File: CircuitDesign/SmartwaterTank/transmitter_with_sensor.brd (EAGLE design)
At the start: 53 x 25.4 mm, 11 parts, among them IC1 MEGA8-P

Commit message: Issue #5: update transmitter schema
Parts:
- added C1, C2: 22pf, rcl:C025-025X050
- added Q1: 455E, special:QS
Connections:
- new net N$10: IC1.6, J_ULTRASONIC_1.ECHO
- new net N$7: C1.1, IC1.9, Q1.2
- new net N$8: C2.1, IC1.10, Q1.1
- new net N$9: IC1.14, U$1.DATA
- net GND: now also C1.2, C2.2
- net N$11: now also IC1.5
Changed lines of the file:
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@@
 <attribute name="VALUE" x="58.42" y="69.18" size="0.0254" layer="27"/>
+</element>
+<element name="Q1" library="special" library_urn="urn:adsk.eagle:library:367" package="QS" package3d_urn="urn:adsk.eagle:package:26647/2" value="455E" x="54.61" y="49.53" smashed="yes">
+<attribute name="NAME" x="49.53" y="52.197" size="1.27" layer="25" ratio="10"/>
+<attribute name="POPULARITY" value="59" x="54.61" y="49.53" size="1.778" layer="27" display="off"/>
+<attribute name="VALUE" x="49.53" y="45.593" size="1.27" layer="27" ratio="10"/>
+</element>
+<element name="C1" library="rcl" library_urn="urn:adsk.eagle:library:334" package="C025-025X050" package3d_urn="urn:adsk.eagle:package:23629/2" value="22pf" x="52.07" y="43.18" smashed="yes">
+<attribute name="NAME" x="49.784" y="44.704" size="1.27" layer="25" ratio="10"/>
+<attribute name="POPULARITY" value="65" x="52.07" y="43.18" size="1.778" layer="27" display="off"/>
+<attribute name="SPICEPREFIX" value="C" x="52.07" y="43.18" size="1.778" layer="27" display="off"/>
+<attribute name="VALUE" x="49.784" y="40.386" size="1.27" layer="27" ratio="10"/>
+</element>
+<element name="C2" library="rcl" library_urn="urn:adsk.eagle:library:334" package="C025-025X050" package3d_urn="urn:adsk.eagle:package:23629/2" value="22pf" x="52.07" y="38.1" smashed="yes">
+<attribute name="NAME" x="49.784" y="39.624" size="1.27" layer="25" ratio="10"/>
+<attribute name="POPULARITY" value="65" x="52.07" y="38.1" size="1.778" layer="27" display="off"/>
+<attribute name="SPICEPREFIX" value="C" x="52.07" y="38.1" size="1.778" layer="27" display="off"/>
+<attribute name="VALUE" x="49.784" y="35.306" size="1.27" layer="27" ratio="10"/>
 </element>
 </elements>
@@
 <signal name="GND">
 <contactref element="IC1" pad="8"/>
+<contactref element="C1" pad="2"/>
+<contactref element="C2" pad="2"/>
+<wire x1="53.34" y1="43.18" x2="81.28" y2="68.58" width="0" layer="19" extent="1-1"/>
+<wire x1="53.34" y1="38.1" x2="53.34" y2="43.18" width="0" layer="19" extent="1-1"/>
 </signal>
 <signal name="AVCC">
@@
 <signal name="N$11">
 <contactref element="J_ULTRASONIC_1" pad="TRIG"/>
+<contactref element="IC1" pad="5"/>
+<wire x1="71.12" y1="62.23" x2="73.66" y2="68.58" width="0" layer="19" extent="1-1"/>
 </signal>
 <signal name="N$1">
@@
 <wire x1="78.74" y1="78.74" x2="78.4606" y2="79.0194" width="0.1524" layer="1"/>
 </signal>
+<signal name="N$7">
+<contactref element="IC1" pad="9"/>
+<contactref element="Q1" pad="2"/>
+<contactref element="C1" pad="1"/>
+<wire x1="57.15" y1="49.53" x2="83.82" y2="68.58" width="0" layer="19" extent="1-1"/>
+<wire x1="50.8" y1="43.18" x2="57.15" y2="49.53" width="0" layer="19" extent="1-1"/>
+</signal>
+<signal name="N$8">
+<contactref element="IC1" pad="10"/>
+<contactref element="Q1" pad="1"/>
+<contactref element="C2" pad="1"/>
+<wire x1="52.07" y1="49.53" x2="86.36" y2="68.58" width="0" layer="19" extent="1-1"/>
+<wire x1="50.8" y1="38.1" x2="52.07" y2="49.53" width="0" layer="19" extent="1-1"/>
+</signal>
+<signal name="N$9">
+<contactref element="IC1" pad="14"/>
+<contactref element="U$1" pad="DATA"/>
+<wire x1="55.88" y1="62.103" x2="96.52" y2="68.58" width="0" layer="19" extent="1-1"/>
+</signal>
+<signal name="N$10">
+<contactref element="IC1" pad="6"/>
+<contactref element="J_ULTRASONIC_1" pad="ECHO"/>
+<wire x1="68.58" y1="62.23" x2="76.2" y2="68.58" width="0" layer="19" extent="1-1"/>
+</signal>
 </signals>

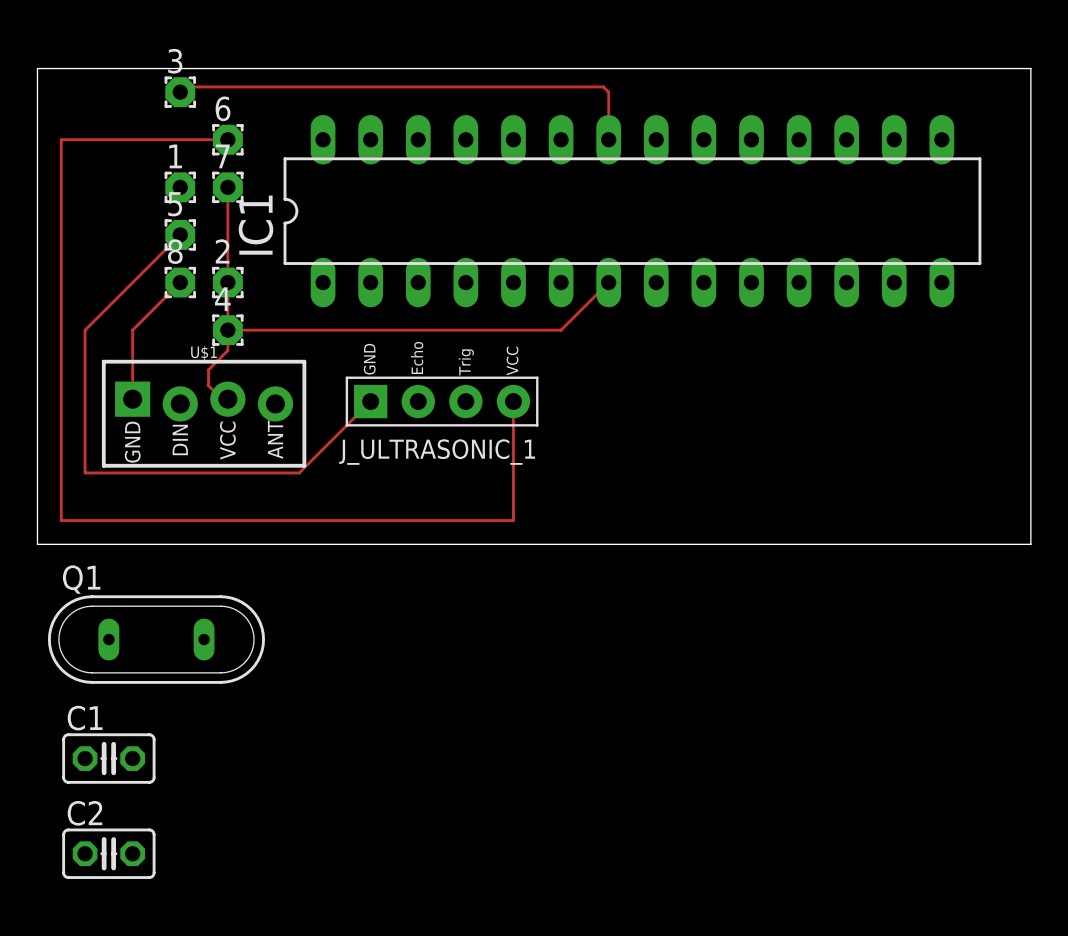
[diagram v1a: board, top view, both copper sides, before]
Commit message: Issue #2: complete transmitter board design for vero board
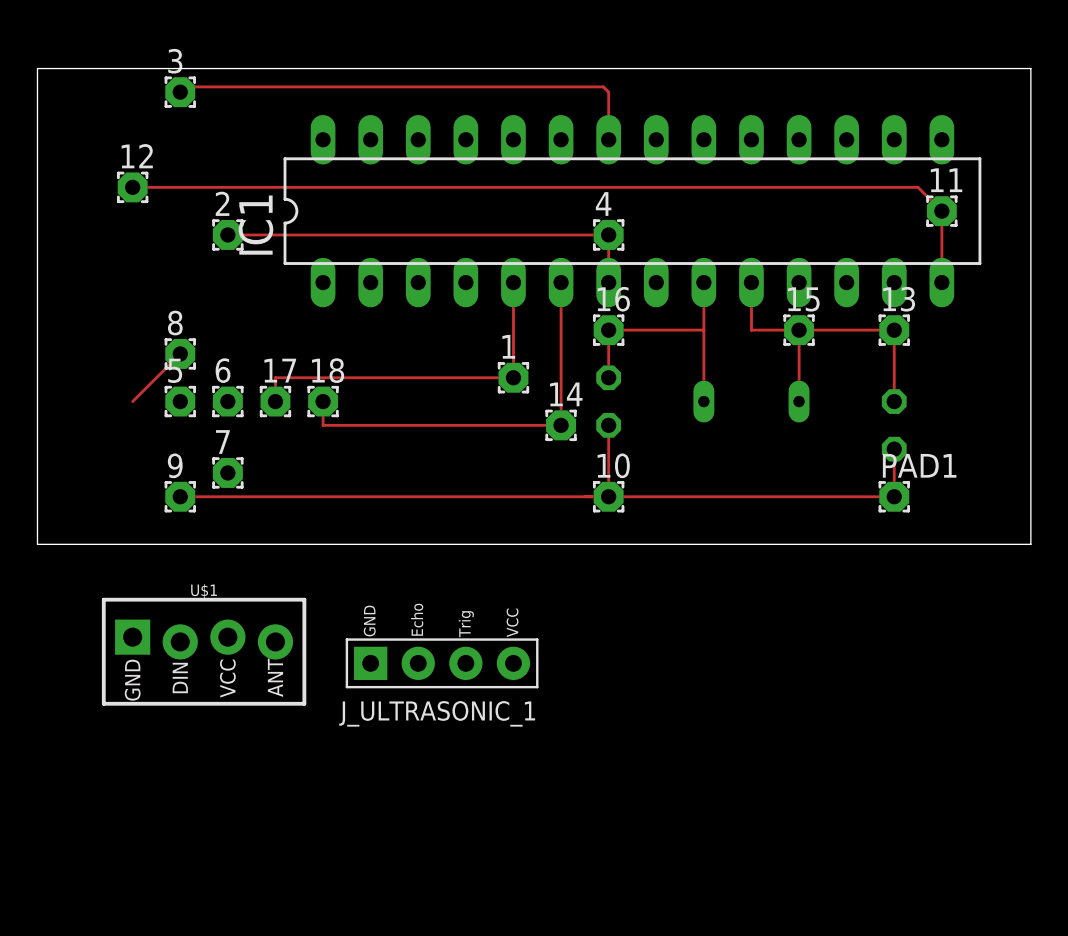
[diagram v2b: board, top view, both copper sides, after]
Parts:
- added 10, 11, 12, 13, 14, 15, 16, 17, 18, 9: WIREPAD1,6/0,8, wirepad:1,6/0,8
- added PAD1: (no value), wirepad:1,6/0,8
- moved C2 47.7 mm to (94.0, 61.0), flipped to the bottom, turned to 270 degrees
- moved Q1 34.2 mm to (86.4, 62.2), flipped to the bottom
- moved C1 32.8 mm to (78.7, 62.2), flipped to the bottom, turned to 270 degrees
- moved 4 20.9 mm to (78.7, 71.1)
- moved 1 20.5 mm to (73.7, 63.5)
- moved 7 15.2 mm to (58.4, 58.4)
- moved 6 14.0 mm to (58.4, 62.2)
- moved J_ULTRASONIC_1 14.0 mm to (69.8, 48.3)
- moved U$1 12.7 mm to (57.1, 49.5)
- moved 5 8.89 mm to (55.9, 62.2)
- moved 8 3.81 mm to (55.9, 64.8)
- moved 2 2.54 mm to (58.4, 71.1)
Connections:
- removed net N$9: IC1.14, U$1.DATA
- new net N$12: 10.1, 9.1, C1.2, C2.2, PAD1.1
- new net N$14: 11.1, 12.1, IC1.14, U$1.DATA
- net GND: no longer C1.2, C2.2
- net N$10: now also 14.1, 18.1
- net N$11: now also 1.1, 17.1
- net N$3: now also 2.1
- net N$7: now also 16.1
- net N$8: now also 13.1, 15.1
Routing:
- net N$1: track 59.7 -> 0.00 mm
- net N$14: track 0.00 -> 47.5 mm
- net N$12: track 0.00 -> 45.7 mm
- net N$4: track 31.6 -> 0.00 mm
- net N$10: track 0.00 -> 21.6 mm
- net N$11: track 0.00 -> 19.0 mm
- net N$8: track 0.00 -> 17.8 mm
- net N$7: track 0.00 -> 14.0 mm
- net N$6: track 12.3 -> 0.18 mm
- net N$5: track 7.28 -> 3.59 mm
- net N$3: track 21.4 -> 22.9 mm

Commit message: Issue #2: remove unnecessary texts from schematic
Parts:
- moved 12 19.0 mm to (53.3, 54.6)
- moved 11 17.8 mm to (96.5, 54.6)
- flipped C1 to the top
- flipped C2 to the top
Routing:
- net N$14: track 47.5 -> 57.1 mm
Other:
- board size 53 x 25.4 mm -> 53 x 26.7 mm
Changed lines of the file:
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@@
 <board>
 <plain>
-<wire x1="48.26" y1="54.61" x2="101.27" y2="54.61" width="0" layer="20"/>
-<wire x1="101.27" y1="54.61" x2="101.27" y2="80" width="0" layer="20"/>
+<wire x1="48.26" y1="53.34" x2="101.27" y2="53.34" width="0" layer="20"/>
+<wire x1="101.27" y1="53.34" x2="101.27" y2="80" width="0" layer="20"/>
 <wire x1="101.27" y1="80" x2="48.26" y2="80" width="0" layer="20"/>
-<wire x1="48.26" y1="80" x2="48.26" y2="54.61" width="0" layer="20"/>
+<wire x1="48.26" y1="80" x2="48.26" y2="53.34" width="0" layer="20"/>
 </plain>
 <attributes>
@@
 <attribute name="VALUE" x="91.44" y="58.293" size="1.27" layer="28" ratio="10" rot="MR0"/>
 </element>
-<element name="C1" library="rcl" library_urn="urn:adsk.eagle:library:334" package="C025-025X050" package3d_urn="urn:adsk.eagle:package:23629/2" value="22pf" x="78.74" y="62.23" smashed="yes" rot="MR270">
-<attribute name="NAME" x="77.216" y="64.516" size="1.27" layer="26" ratio="10" rot="MR270"/>
-<attribute name="POPULARITY" value="65" x="78.74" y="62.23" size="1.778" layer="28" rot="MR270" display="off"/>
-<attribute name="SPICEPREFIX" value="C" x="78.74" y="62.23" size="1.778" layer="28" rot="MR270" display="off"/>
-<attribute name="VALUE" x="81.534" y="64.516" size="1.27" layer="28" ratio="10" rot="MR270"/>
-</element>
-<element name="C2" library="rcl" library_urn="urn:adsk.eagle:library:334" package="C025-025X050" package3d_urn="urn:adsk.eagle:package:23629/2" value="22pf" x="93.98" y="60.96" smashed="yes" rot="MR270">
-<attribute name="NAME" x="92.456" y="63.246" size="1.27" layer="26" ratio="10" rot="MR270"/>
-<attribute name="POPULARITY" value="65" x="93.98" y="60.96" size="1.778" layer="28" rot="MR270" display="off"/>
-<attribute name="SPICEPREFIX" value="C" x="93.98" y="60.96" size="1.778" layer="28" rot="MR270" display="off"/>
-<attribute name="VALUE" x="96.774" y="63.246" size="1.27" layer="28" ratio="10" rot="MR270"/>
+<element name="C1" library="rcl" library_urn="urn:adsk.eagle:library:334" package="C025-025X050" package3d_urn="urn:adsk.eagle:package:23629/2" value="22pf" x="78.74" y="62.23" smashed="yes" rot="R270">
+<attribute name="NAME" x="80.264" y="64.516" size="1.27" layer="25" ratio="10" rot="R270"/>
+<attribute name="POPULARITY" value="65" x="78.74" y="62.23" size="1.778" layer="27" rot="R270" display="off"/>
+<attribute name="SPICEPREFIX" value="C" x="78.74" y="62.23" size="1.778" layer="27" rot="R270" display="off"/>
+<attribute name="VALUE" x="75.946" y="64.516" size="1.27" layer="27" ratio="10" rot="R270"/>
+</element>
+<element name="C2" library="rcl" library_urn="urn:adsk.eagle:library:334" package="C025-025X050" package3d_urn="urn:adsk.eagle:package:23629/2" value="22pf" x="93.98" y="60.96" smashed="yes" rot="R270">
+<attribute name="NAME" x="95.504" y="63.246" size="1.27" layer="25" ratio="10" rot="R270"/>
+<attribute name="POPULARITY" value="65" x="93.98" y="60.96" size="1.778" layer="27" rot="R270" display="off"/>
+<attribute name="SPICEPREFIX" value="C" x="93.98" y="60.96" size="1.778" layer="27" rot="R270" display="off"/>
+<attribute name="VALUE" x="91.186" y="63.246" size="1.27" layer="27" ratio="10" rot="R270"/>
 </element>
 <element name="9" library="wirepad" library_urn="urn:adsk.eagle:library:412" package="1,6/0,8" package3d_urn="urn:adsk.eagle:package:30830/1" value="WIREPAD1,6/0,8" x="55.88" y="57.15" smashed="yes">
@@
 <attribute name="VALUE" x="93.98" y="57.75" size="0.0254" layer="27"/>
 </element>
-<element name="11" library="wirepad" library_urn="urn:adsk.eagle:library:412" package="1,6/0,8" package3d_urn="urn:adsk.eagle:package:30830/1" value="WIREPAD1,6/0,8" x="96.52" y="72.39" smashed="yes">
-<attribute name="NAME" x="95.758" y="73.406" size="1.27" layer="25" ratio="10"/>
-<attribute name="POPULARITY" value="1" x="96.52" y="72.39" size="1.778" layer="27" display="off"/>
-<attribute name="VALUE" x="96.52" y="72.99" size="0.0254" layer="27"/>
-</element>
-<element name="12" library="wirepad" library_urn="urn:adsk.eagle:library:412" package="1,6/0,8" package3d_urn="urn:adsk.eagle:package:30830/1" value="WIREPAD1,6/0,8" x="53.34" y="73.66" smashed="yes">
-<attribute name="NAME" x="52.578" y="74.676" size="1.27" layer="25" ratio="10"/>
-<attribute name="POPULARITY" value="1" x="53.34" y="73.66" size="1.778" layer="27" display="off"/>
-<attribute name="VALUE" x="53.34" y="74.26" size="0.0254" layer="27"/>
+<element name="11" library="wirepad" library_urn="urn:adsk.eagle:library:412" package="1,6/0,8" package3d_urn="urn:adsk.eagle:package:30830/1" value="WIREPAD1,6/0,8" x="96.52" y="54.61" smashed="yes">
+<attribute name="NAME" x="95.758" y="55.626" size="1.27" layer="25" ratio="10"/>
+<attribute name="POPULARITY" value="1" x="96.52" y="54.61" size="1.778" layer="27" display="off"/>
+<attribute name="VALUE" x="96.52" y="55.21" size="0.0254" layer="27"/>
+</element>
+<element name="12" library="wirepad" library_urn="urn:adsk.eagle:library:412" package="1,6/0,8" package3d_urn="urn:adsk.eagle:package:30830/1" value="WIREPAD1,6/0,8" x="53.34" y="54.61" smashed="yes">
+<attribute name="NAME" x="52.578" y="55.626" size="1.27" layer="25" ratio="10"/>
+<attribute name="POPULARITY" value="1" x="53.34" y="54.61" size="1.778" layer="27" display="off"/>
+<attribute name="VALUE" x="53.34" y="55.21" size="0.0254" layer="27"/>
 </element>
 <element name="13" library="wirepad" library_urn="urn:adsk.eagle:library:412" package="1,6/0,8" package3d_urn="urn:adsk.eagle:package:30830/1" value="WIREPAD1,6/0,8" x="93.98" y="66.04" smashed="yes">
@@
 <wire x1="83.82" y1="66.04" x2="83.82" y2="62.23" width="0.1524" layer="1"/>
 <wire x1="78.74" y1="66.04" x2="83.82" y2="66.04" width="0.1524" layer="1"/>
-<wire x1="78.74" y1="66.04" x2="78.74" y2="63.5" width="0.1524" layer="1"/>
+<wire x1="78.74" y1="66.04" x2="78.74" y2="63.5" width="0.1524" layer="16"/>
 </signal>
 <signal name="N$8">
@@
 <contactref element="13" pad="1"/>
 <wire x1="88.9" y1="66.04" x2="93.98" y2="66.04" width="0.1524" layer="1"/>
-<wire x1="93.98" y1="66.04" x2="93.98" y2="62.23" width="0.1524" layer="1"/>
+<wire x1="93.98" y1="66.04" x2="93.98" y2="62.23" width="0.1524" layer="16"/>
 </signal>
 <signal name="N$10">
@@
 <contactref element="C1" pad="2"/>
 <contactref element="10" pad="1"/>
-<wire x1="78.74" y1="60.96" x2="78.74" y2="57.15" width="0.1524" layer="1"/>
+<wire x1="78.74" y1="60.96" x2="78.74" y2="57.15" width="0.1524" layer="16"/>
 <contactref element="C2" pad="2"/>
 <contactref element="PAD1" pad="1"/>
-<wire x1="93.98" y1="59.69" x2="93.98" y2="57.15" width="0.1524" layer="1"/>
+<wire x1="93.98" y1="59.69" x2="93.98" y2="57.15" width="0.1524" layer="16"/>
 <wire x1="93.98" y1="57.15" x2="78.74" y2="57.15" width="0.1524" layer="1"/>
 <contactref element="9" pad="1"/>
@@
 <contactref element="U$1" pad="DATA"/>
 <contactref element="12" pad="1"/>
-<wire x1="96.52" y1="68.58" x2="96.52" y2="72.39" width="0.1524" layer="1"/>
-<wire x1="96.52" y1="72.39" x2="95.25" y2="73.66" width="0.1524" layer="1"/>
-<wire x1="95.25" y1="73.66" x2="53.34" y2="73.66" width="0.1524" layer="1"/>
-<wire x1="55.88" y1="49.403" x2="53.34" y2="73.66" width="0" layer="19" extent="1-1"/>
+<wire x1="96.52" y1="68.58" x2="96.52" y2="54.61" width="0.1524" layer="1"/>
+<wire x1="96.52" y1="54.61" x2="53.34" y2="54.61" width="0.1524" layer="1"/>
+<wire x1="55.88" y1="49.403" x2="53.34" y2="54.61" width="0" layer="19" extent="1-1"/>
 </signal>
 <signal name="N$3">

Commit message: Issue #2: update schema and board
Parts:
- removed 10, 12, 13, 15, 16, 17, 18, 2, 3, 9: WIREPAD1,6/0,8, wirepad:1,6/0,8
- removed C1, C2: 22pf, rcl:C025-025X050
- removed PAD1: (no value), wirepad:1,6/0,8
- removed Q1: 455E, special:QS
- added 19, 20, DATA, ECHO, G, G2, MISO, MOSI, RESET, SCK, TRIG, V: WIREPAD1,6/0,8, wirepad:1,6/0,8
- added Y1: 32.768kHz, SparkFun-Clocks:CRYSTAL-PTH-2X6-CYL
- moved 4 8.89 mm to (78.7, 62.2)
- moved 1 8.89 mm to (73.7, 54.6)
- moved 11 8.89 mm to (96.5, 45.7)
- moved 14 8.89 mm to (76.2, 52.1)
- moved 7 8.89 mm to (58.4, 49.5)
- moved IC1 8.89 mm to (80.0, 63.5)
- moved J_ULTRASONIC_1 8.89 mm to (69.8, 39.4)
- moved U$1 8.89 mm to (57.1, 40.6)
- moved 5 8.89 mm to (55.9, 53.3)
- moved 6 8.89 mm to (58.4, 53.3)
- moved 8 8.89 mm to (55.9, 55.9)
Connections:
- new net N$13: IC1.18, MISO.1
- new net N$15: IC1.19, SCK.1
- new net N$9: 19.1, 20.1, IC1.1, RESET.1
- net N$10: now also ECHO.1; no longer 18.1
- net N$11: now also TRIG.1; no longer 17.1
- net N$12: now also IC1.17, MOSI.1; no longer 10.1, 9.1, C1.2, C2.2, PAD1.1
- net N$14: now also DATA.1; no longer 12.1
- net N$2: now also G.1, G2.1; no longer 3.1
- net N$3: now also V.1; no longer 2.1
- net N$7: now also Y1.2; no longer 16.1, C1.1, Q1.2
- net N$8: now also Y1.1; no longer 13.1, 15.1, C2.1, Q1.1
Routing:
- net N$12: track 45.7 -> 5.08 mm
- net N$9: track 0.00 -> 22.9 mm
- net N$2: track 25.6 -> 33.0 mm
- net N$8: track 17.8 -> 11.4 mm
- net N$15: track 0.00 -> 5.08 mm
- net N$13: track 0.00 -> 5.08 mm
- net N$7: track 14.0 -> 11.4 mm
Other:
- board size 53 x 26.7 mm -> 53 x 30.5 mm
